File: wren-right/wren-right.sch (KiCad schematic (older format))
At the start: 93 parts, among them J1 TRRS_Jack, SW0 Reset, U1 ProMicro

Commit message: Tracks Finished
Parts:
- MX41: footprint MX_Only:MX-2U -> MX_Only:MX-2U-FLIPPED-ReversedStabilizers
- SW0: footprint random-keyboard-parts:SKQG-1155865 -> Button_Switch_THT:SW_PUSH_6mm
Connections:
- net COL0: now also U1.13 (D10(PB6)); no longer U1.20 (A3(PF4))
- net COL1: now also U1.14 (D16(PB2)); no longer U1.19 (A2(PF5))
- net COL2: now also U1.15 (D14(PB3)); no longer U1.18 (A1(PF6))
- net COL3: now also U1.16 (D15(PB1)); no longer U1.17 (A0(PF7))
- net COL4: now also U1.17 (A0(PF7)); no longer U1.16 (D15(PB1))
- net COL5: now also U1.18 (A1(PF6)); no longer U1.15 (D14(PB3))
- net COL6: now also U1.19 (A2(PF5)); no longer U1.14 (D16(PB2))
- net COL7: now also U1.20 (A3(PF4)); no longer U1.13 (D10(PB6))
- net COL8: now also U1.9 (D6(PD7)); no longer U1.1 (TX(PD3))
- net COL9: now also U1.10 (D7(PE6)); no longer U1.2 (RX(PD2))
- net ROW0: now also U1.1 (TX(PD3)); no longer U1.7 (D4(PD4))
- net ROW1: now also U1.2 (RX(PD2)); no longer U1.8 (D5(PC6))
- net ROW2: now also U1.7 (D4(PD4)); no longer U1.9 (D6(PD7))
- net ROW3: now also U1.8 (D5(PC6)); no longer U1.10 (D7(PE6))
- net ROW4: now also U1.12 (D9(PB5)); no longer U1.11 (D8(PB4))
- no-connect marks 1 -> 2
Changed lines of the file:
@@
 Text GLabel 1950 3150 0    50   BiDi ~ 0
-SCL
-Text GLabel 3950 4250 2    50   BiDi ~ 0
-SDA
-Text GLabel 3950 4350 2    50   BiDi ~ 0
 SCL
 Text GLabel 3250 2950 2    50   Output ~ 0
@@
 	1    0    0    -1
 $EndComp
-$Comp
-L Device:R_Small R2
-U 1 1 6072E460
-P 3500 4450
-F 0 "R2" H 3559 4496 50  0000 L CNN
-F 1 "10kOhms" H 3559 4405 50  0000 L CNN
-F 2 "Resistor_SMD:R_0805_2012Metric" H 3500 4450 50  0001 C CNN
-F 3 "~" H 3500 4450 50  0001 C CNN
-	1    3500 4450
-	1    0    0    -1
-$EndComp
 Wire Wire Line
 	2850 4450 3000 4450
@@
 F 0 "SW0" H 3750 3135 50  0000 C CNN
 F 1 "Reset" H 3750 3044 50  0000 C CNN
-F 2 "random-keyboard-parts:SKQG-1155865" H 3750 3050 50  0001 C CNN
+F 2 "Button_Switch_THT:SW_PUSH_6mm" H 3750 3050 50  0001 C CNN
 F 3 "~" H 3750 3050 50  0001 C CNN
 	1    3750 2850
@@
 F 0 "MX41" H 5133 5773 60  0000 C CNN
 F 1 "MX-NoLED" H 5133 5699 20  0000 C CNN
-F 2 "MX_Only:MX-2U" H 4475 5525 60  0001 C CNN
+F 2 "MX_Only:MX-2U-FLIPPED-ReversedStabilizers" H 4475 5525 60  0001 C CNN
 F 3 "" H 4475 5525 60  0001 C CNN
 	1    5100 5550
@@
 Text GLabel 9750 2350 1    50   Input ~ 0
 COL9
+Text GLabel 3250 3750 2    50   Input ~ 0
+COL0
+Text GLabel 3250 3650 2    50   Input ~ 0
+COL1
+Text GLabel 3250 3550 2    50   Input ~ 0
+COL2
+Text GLabel 3250 3450 2    50   Input ~ 0
+COL3
+Text GLabel 3250 3350 2    50   Input ~ 0
+COL4
+Text GLabel 3250 3250 2    50   Input ~ 0
+COL5
+Text GLabel 3250 3150 2    50   Input ~ 0
+COL6
 Text GLabel 3250 3050 2    50   Input ~ 0
-COL0
-Text GLabel 3250 3150 2    50   Input ~ 0
-COL1
-Text GLabel 3250 3250 2    50   Input ~ 0
-COL2
-Text GLabel 3250 3350 2    50   Input ~ 0
-COL3
-Text GLabel 3250 3450 2    50   Input ~ 0
-COL4
-Text GLabel 3250 3550 2    50   Input ~ 0
-COL5
-Text GLabel 3250 3650 2    50   Input ~ 0
-COL6
-Text GLabel 3250 3750 2    50   Input ~ 0
 COL7
+Text GLabel 1950 3450 0    50   Input ~ 0
+COL8
+Text GLabel 1950 3550 0    50   Input ~ 0
+COL9
 Text GLabel 1950 2650 0    50   Input ~ 0
-COL8
+ROW0
 Text GLabel 1950 2750 0    50   Input ~ 0
-COL9
+ROW1
 Text GLabel 1950 3250 0    50   Input ~ 0
-ROW0
+ROW2
 Text GLabel 1950 3350 0    50   Input ~ 0
-ROW1
-Text GLabel 1950 3450 0    50   Input ~ 0
-ROW2
-Text GLabel 1950 3550 0    50   Input ~ 0
 ROW3
-Text GLabel 1950 3650 0    50   Input ~ 0
+Text GLabel 1950 3750 0    50   Input ~ 0
 ROW4
-NoConn ~ 1950 3750
+NoConn ~ 1950 3650
+NoConn ~ 1850 4650
+$Comp
+L Device:R_Small R2
+U 1 1 6072E460
+P 3500 4450
+F 0 "R2" H 3559 4496 50  0000 L CNN
+F 1 "10kOhms" H 3559 4405 50  0000 L CNN
+F 2 "Resistor_SMD:R_0805_2012Metric" H 3500 4450 50  0001 C CNN
+F 3 "~" H 3500 4450 50  0001 C CNN
+	1    3500 4450
+	1    0    0    -1
+$EndComp
+Text GLabel 3950 4350 2    50   BiDi ~ 0
+SCL
+Text GLabel 3950 4250 2    50   BiDi ~ 0
+SDA
 $EndSCHEMATC

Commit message: Left Side Finished
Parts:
- removed D10, D17, D18, D19, D20, D27, D28, D29, D30, D37, D38, D39, D40, D7, D8, D9: D_Small, Diode_SMD:D_SOD-123, symbol Device:D_Small
- removed MX10, MX17, MX18, MX19, MX20, MX27, MX28, MX29, MX30, MX37, MX38, MX39, MX40, MX7, MX8, MX9: MX-NoLED, MX_Only:MX-1U, symbol MX_Alps_Hybrid:MX-NoLED
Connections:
- net ROW4: no longer U1.12 (D9(PB5))
- net COL6: no longer names the net of U1.19 (A2(PF5))
- net COL7: no longer names the net of U1.20 (A3(PF4))
- net COL8: no longer names the net of U1.9 (D6(PD7))
- net COL9: no longer names the net of U1.10 (D7(PE6))
- no-connect marks 2 -> 6

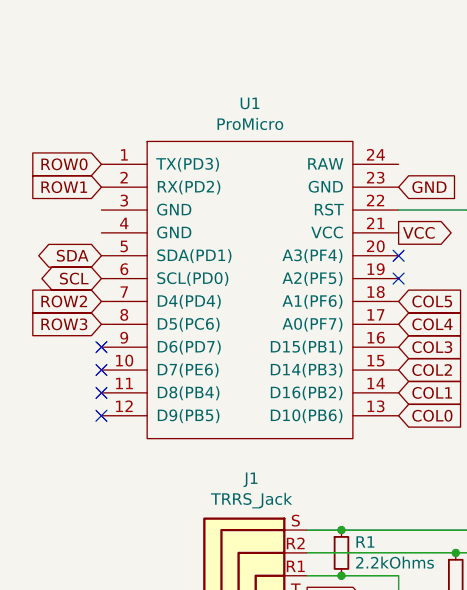
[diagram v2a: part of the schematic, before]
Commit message: Added Mirrored Right PCB
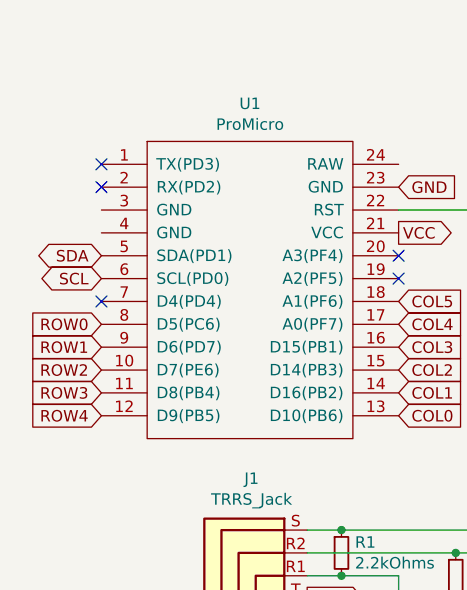
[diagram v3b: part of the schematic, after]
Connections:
- net ROW0: now also U1.8 (D5(PC6)); no longer U1.1 (TX(PD3))
- net ROW1: now also U1.9 (D6(PD7)); no longer U1.2 (RX(PD2))
- net ROW2: now also U1.10 (D7(PE6)); no longer U1.7 (D4(PD4))
- net ROW3: now also U1.11 (D8(PB4)); no longer U1.8 (D5(PC6))
- net ROW4: now also U1.12 (D9(PB5))
- no-connect marks 6 -> 5
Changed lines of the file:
@@
 Text GLabel 3250 3350 2    50   Input ~ 0
 COL4
-Text GLabel 3250 3250 2    50   Input ~ 0
-COL5
-Text GLabel 1950 2650 0    50   Input ~ 0
-ROW0
-Text GLabel 1950 2750 0    50   Input ~ 0
-ROW1
-Text GLabel 1950 3250 0    50   Input ~ 0
+Text GLabel 1950 3550 0    50   Input ~ 0
 ROW2
-Text GLabel 1950 3350 0    50   Input ~ 0
+Text GLabel 1950 3650 0    50   Input ~ 0
 ROW3
-NoConn ~ 1950 3650
+Text GLabel 1950 3750 0    50   Input ~ 0
+ROW4
 $Comp
 L Device:R_Small R2
@@
 Text GLabel 3950 4250 2    50   BiDi ~ 0
 SDA
+Text GLabel 1950 3450 0    50   Input ~ 0
+ROW1
+Text GLabel 1950 3350 0    50   Input ~ 0
+ROW0
+Text GLabel 3250 3250 2    50   Input ~ 0
+COL5
+NoConn ~ 3250 3150
 NoConn ~ 3250 3050
-NoConn ~ 3250 3150
-NoConn ~ 1950 3750
-NoConn ~ 1950 3550
-NoConn ~ 1950 3450
+NoConn ~ 1950 3250
+NoConn ~ 1950 2750
+NoConn ~ 1950 2650
 $EndSCHEMATC

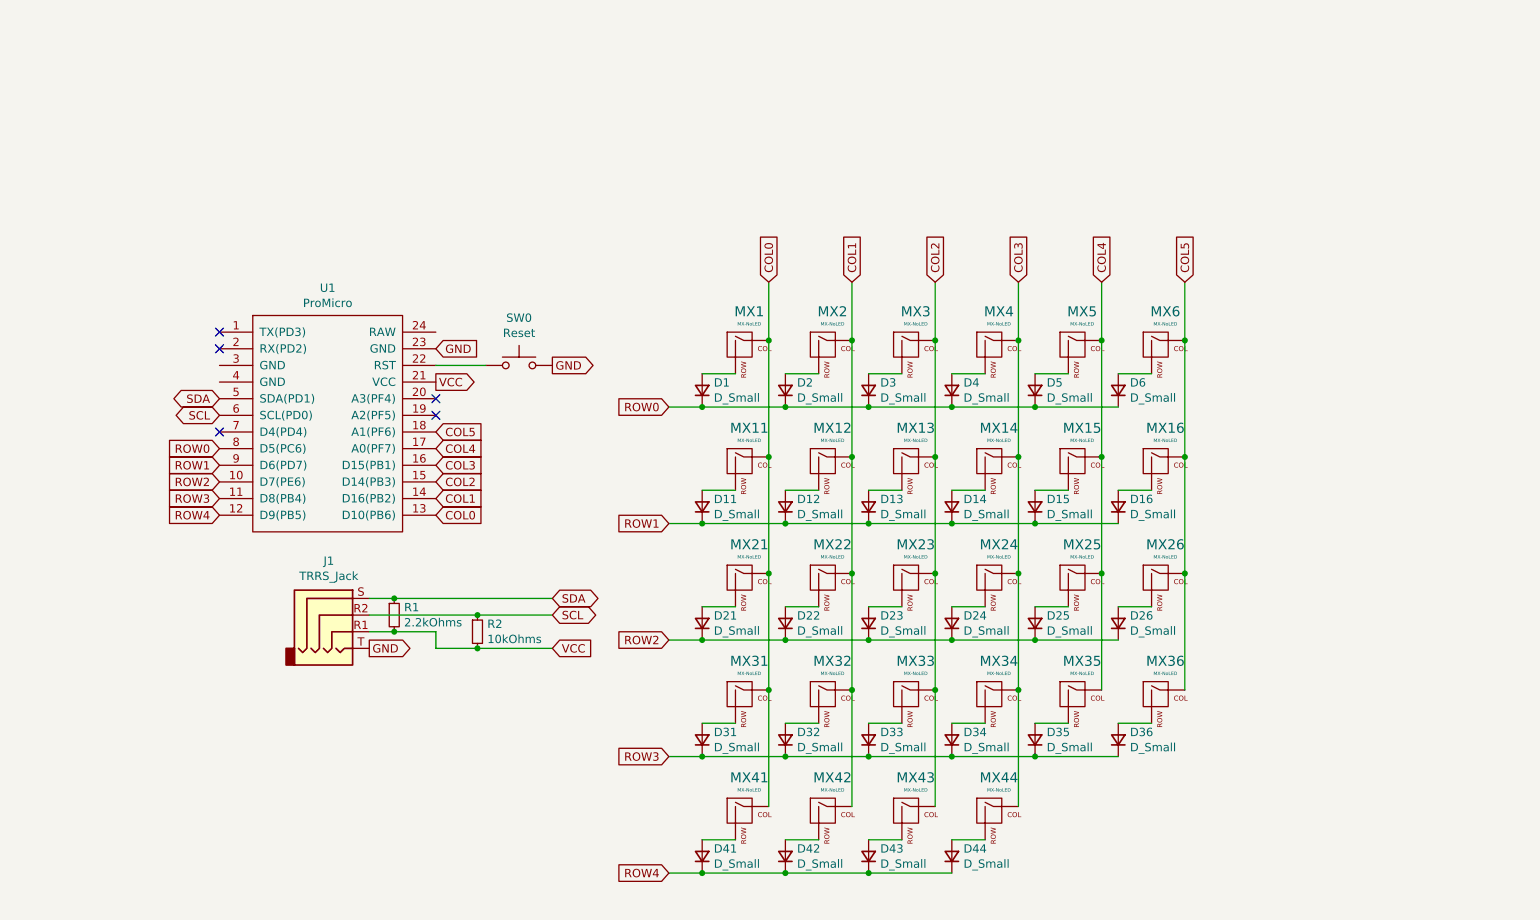
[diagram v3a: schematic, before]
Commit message: Add encoder to right side of schematic
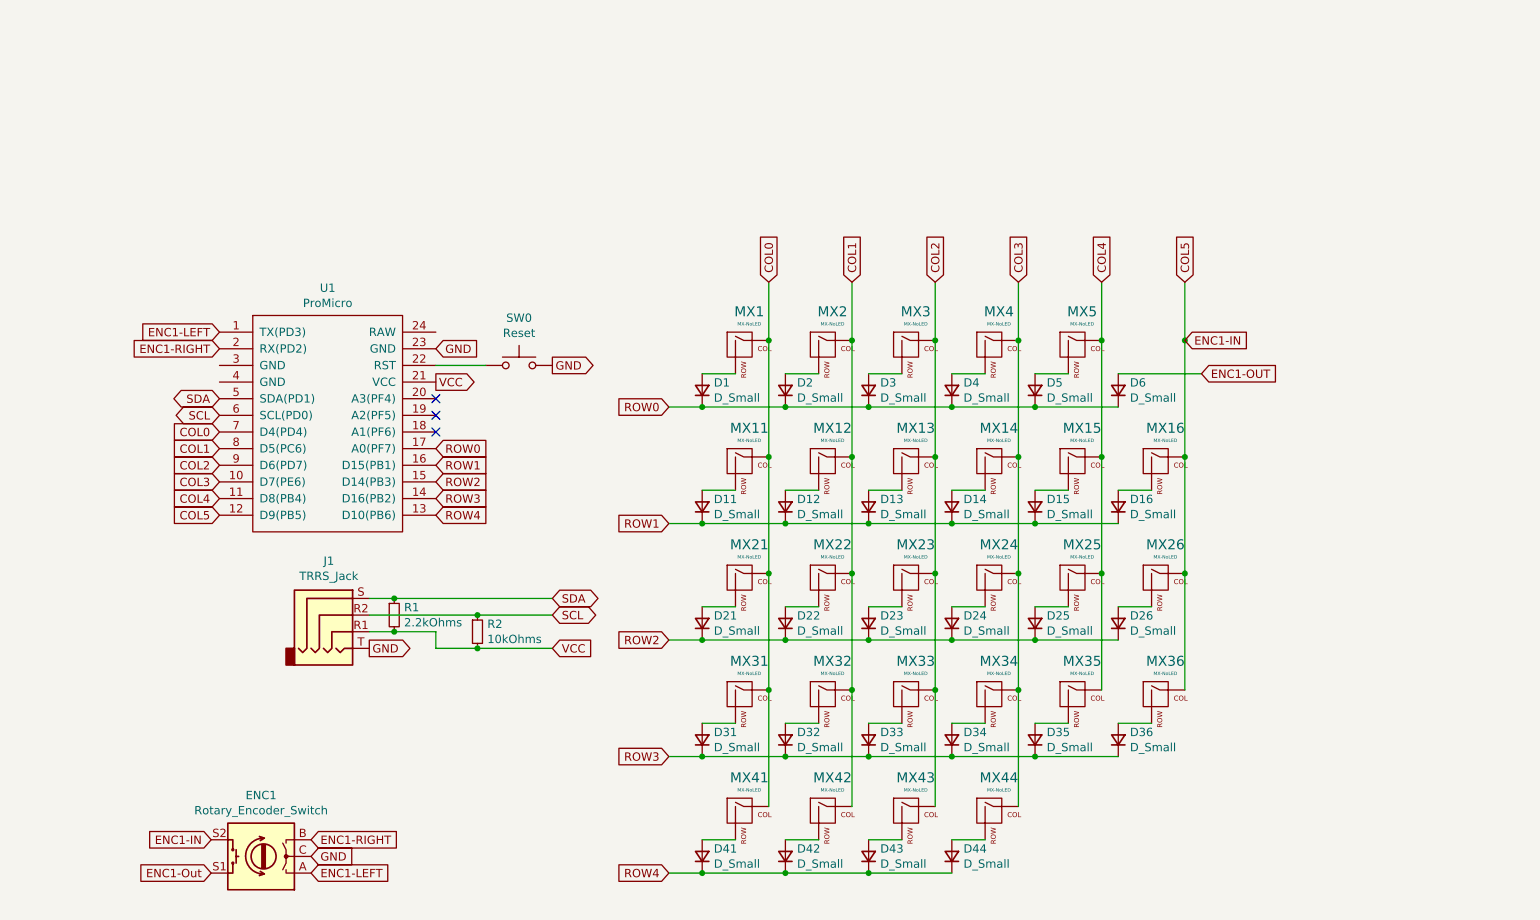
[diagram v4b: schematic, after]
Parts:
- removed MX6: MX-NoLED, MX_Only:MX-1U, symbol MX_Alps_Hybrid:MX-NoLED
- added ENC1: Rotary_Encoder_Switch, symbol Device:Rotary_Encoder_Switch
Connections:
- net COL0: now also U1.7 (D4(PD4)); no longer U1.13 (D10(PB6))
- net COL1: now also U1.8 (D5(PC6)); no longer U1.14 (D16(PB2))
- net COL2: now also U1.9 (D6(PD7)); no longer U1.15 (D14(PB3))
- net COL3: now also U1.10 (D7(PE6)); no longer U1.16 (D15(PB1))
- net COL4: now also U1.11 (D8(PB4)); no longer U1.17 (A0(PF7))
- net COL5: now also U1.12 (D9(PB5)), ENC1.S2; no longer U1.18 (A1(PF6))
- net GND: now also ENC1.C
- net ROW0: now also U1.17 (A0(PF7)); no longer U1.8 (D5(PC6))
- net ROW1: now also U1.16 (D15(PB1)); no longer U1.9 (D6(PD7))
- net ROW2: now also U1.15 (D14(PB3)); no longer U1.10 (D7(PE6))
- net ROW3: now also U1.14 (D16(PB2)); no longer U1.11 (D8(PB4))
- net ROW4: now also U1.13 (D10(PB6)); no longer U1.12 (D9(PB5))
- net ENC1-LEFT: now reaches U1.1 (TX(PD3))
- net ENC1-LEFT: now also ENC1.A
- net ENC1-RIGHT: now reaches U1.2 (RX(PD2))
- net ENC1-RIGHT: now also ENC1.B
- net ENC1-OUT: now reaches D6.2 (A)
- new net ENC1-Out: ENC1.S1
- no-connect marks 5 -> 3
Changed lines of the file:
@@
-	1    0    0    -1
-$EndComp
-$Comp
-L random-keyboard-parts:ProMicro_2 U1
-U 1 1 6071F7CA
-P 2600 3200
-F 0 "U1" H 2600 4015 50  0000 C CNN
-F 1 "ProMicro" H 2600 3924 50  0000 C CNN
-F 2 "footprints:ARDUINO_PRO_MICRO" H 2550 3300 50  0001 C CNN
-F 3 "" H 2550 3300 50  0001 C CNN
-	1    2600 3200
 	1    0    0    -1
 $EndComp
@@
 $EndComp
 $Comp
-L MX_Alps_Hybrid:MX-NoLED MX6
-U 1 1 60752EBC
-P 7600 2750
-F 0 "MX6" H 7633 2973 60  0000 C CNN
-F 1 "MX-NoLED" H 7633 2899 20  0000 C CNN
-F 2 "MX_Only:MX-1U" H 6975 2725 60  0001 C CNN
-F 3 "" H 6975 2725 60  0001 C CNN
-	1    7600 2750
-	1    0    0    -1
-$EndComp
-$Comp
 L MX_Alps_Hybrid:MX-NoLED MX11
 U 1 1 60757491
@@
 	6850 2900 7050 2900
 Wire Wire Line
-	7350 2900 7550 2900
-Wire Wire Line
 	4850 3600 5050 3600
 Wire Wire Line
@@
 Wire Wire Line
 	7250 4100 7250 3400
-Wire Wire Line
-	7750 2350 7750 2700
-Connection ~ 7750 2700
-Wire Wire Line
-	7750 2700 7750 3400
 Connection ~ 7750 3400
 Wire Wire Line
@@
 Text GLabel 7750 2350 1    50   Input ~ 0
 COL5
+Text GLabel 1950 3250 0    50   Input ~ 0
+COL0
+Text GLabel 1950 3350 0    50   Input ~ 0
+COL1
+Text GLabel 1950 3450 0    50   Input ~ 0
+COL2
+Text GLabel 1950 3550 0    50   Input ~ 0
+COL3
+Text GLabel 1950 3650 0    50   Input ~ 0
+COL4
+Text GLabel 3250 3550 2    50   Input ~ 0
+ROW2
+Text GLabel 3250 3650 2    50   Input ~ 0
+ROW3
 Text GLabel 3250 3750 2    50   Input ~ 0
-COL0
-Text GLabel 3250 3650 2    50   Input ~ 0
-COL1
-Text GLabel 3250 3550 2    50   Input ~ 0
-COL2
-Text GLabel 3250 3450 2    50   Input ~ 0
-COL3
-Text GLabel 3250 3350 2    50   Input ~ 0
-COL4
-Text GLabel 1950 3550 0    50   Input ~ 0
-ROW2
-Text GLabel 1950 3650 0    50   Input ~ 0
-ROW3
-Text GLabel 1950 3750 0    50   Input ~ 0
 ROW4
 $Comp
@@
 Text GLabel 3950 4250 2    50   BiDi ~ 0
 SDA
-Text GLabel 1950 3450 0    50   Input ~ 0
+Text GLabel 3250 3450 2    50   Input ~ 0
 ROW1
-Text GLabel 1950 3350 0    50   Input ~ 0
+Text GLabel 3250 3350 2    50   Input ~ 0
 ROW0
-Text GLabel 3250 3250 2    50   Input ~ 0
-COL5
 NoConn ~ 3250 3150
 NoConn ~ 3250 3050
-NoConn ~ 1950 3250
-NoConn ~ 1950 2750
-NoConn ~ 1950 2650
+Text GLabel 1950 3750 0    50   Input ~ 0
+COL5
+$Comp
+L Device:Rotary_Encoder_Switch ENC1
+U 1 1 60751B50
+P 2200 5800
+F 0 "ENC1" H 2200 5433 50  0000 C CNN
+F 1 "Rotary_Encoder_Switch" H 2200 5524 50  0000 C CNN
+F 2 "" H 2050 5960 50  0001 C CNN
+F 3 "~" H 2200 6060 50  0001 C CNN
+	1    2200 5800
+	-1   0    0    1
+$EndComp
+NoConn ~ 3250 3250
+Text GLabel 7750 2700 2    50   Input ~ 0
+ENC1-IN
+Text GLabel 7850 2900 2    50   Input ~ 0
+ENC1-OUT
+Wire Wire Line
+	7350 2900 7850 2900
+Wire Wire Line
+	7750 2350 7750 2700
+Connection ~ 7750 2700
+Wire Wire Line
+	7750 2700 7750 3400
+Text GLabel 1900 5700 0    50   Input ~ 0
+ENC1-IN
+Text GLabel 1900 5900 0    50   Input ~ 0
+ENC1-Out
+Text GLabel 2500 5800 2    50   Input ~ 0
+GND
+Text GLabel 2500 5700 2    50   Input ~ 0
+ENC1-RIGHT
+Text GLabel 2500 5900 2    50   Input ~ 0
+ENC1-LEFT
+$Comp
+L random-keyboard-parts:ProMicro_2 U1
+U 1 1 6071F7CA
+P 2600 3200
+F 0 "U1" H 2600 4015 50  0000 C CNN
+F 1 "ProMicro" H 2600 3924 50  0000 C CNN
+F 2 "footprints:ARDUINO_PRO_MICRO" H 2550 3300 50  0001 C CNN
+F 3 "" H 2550 3300 50  0001 C CNN
+	1    2600 3200
+	1    0    0    -1
+$EndComp
+Text GLabel 1950 2650 0    50   Input ~ 0
+ENC1-LEFT
+Text GLabel 1950 2750 0    50   Input ~ 0
+ENC1-RIGHT
 $EndSCHEMATC

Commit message: Cleaner Track Routing, Remove Encoder
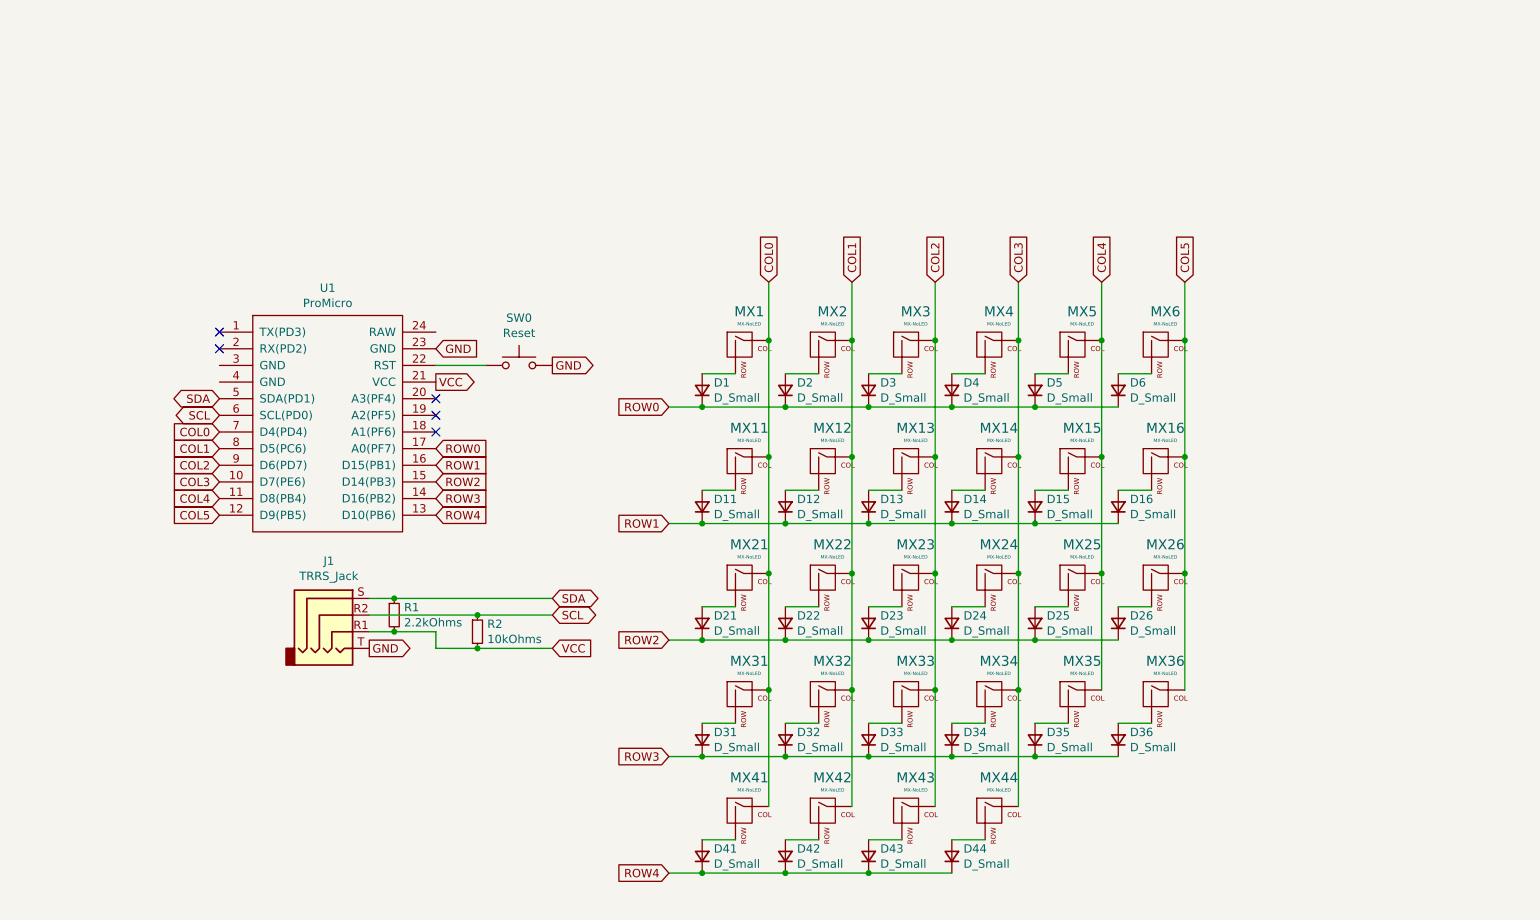
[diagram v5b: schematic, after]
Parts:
- removed ENC1: Rotary_Encoder_Switch, symbol Device:Rotary_Encoder_Switch
- added MX6: MX-NoLED, MX_Only:MX-1U, symbol MX_Alps_Hybrid:MX-NoLED
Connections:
- net COL5: now also MX6.1 (COL)
- net ENC1-LEFT: no longer names the net of U1.1 (TX(PD3))
- net ENC1-OUT: no longer names the net of D6.2 (A)
- net ENC1-OUT: now also MX6.2 (ROW)
- net ENC1-RIGHT: no longer names the net of U1.2 (RX(PD2))
- no-connect marks 3 -> 5
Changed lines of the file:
@@
 Text GLabel 1950 3750 0    50   Input ~ 0
 COL5
-$Comp
-L Device:Rotary_Encoder_Switch ENC1
-U 1 1 60751B50
-P 2200 5800
-F 0 "ENC1" H 2200 5433 50  0000 C CNN
-F 1 "Rotary_Encoder_Switch" H 2200 5524 50  0000 C CNN
-F 2 "" H 2050 5960 50  0001 C CNN
-F 3 "~" H 2200 6060 50  0001 C CNN
-	1    2200 5800
-	-1   0    0    1
-$EndComp
 NoConn ~ 3250 3250
-Text GLabel 7750 2700 2    50   Input ~ 0
-ENC1-IN
-Text GLabel 7850 2900 2    50   Input ~ 0
-ENC1-OUT
-Wire Wire Line
-	7350 2900 7850 2900
-Wire Wire Line
-	7750 2350 7750 2700
-Connection ~ 7750 2700
-Wire Wire Line
-	7750 2700 7750 3400
-Text GLabel 1900 5700 0    50   Input ~ 0
-ENC1-IN
-Text GLabel 1900 5900 0    50   Input ~ 0
-ENC1-Out
-Text GLabel 2500 5800 2    50   Input ~ 0
-GND
-Text GLabel 2500 5700 2    50   Input ~ 0
-ENC1-RIGHT
-Text GLabel 2500 5900 2    50   Input ~ 0
-ENC1-LEFT
 $Comp
 L random-keyboard-parts:ProMicro_2 U1
@@
 	1    0    0    -1
 $EndComp
-Text GLabel 1950 2650 0    50   Input ~ 0
-ENC1-LEFT
-Text GLabel 1950 2750 0    50   Input ~ 0
-ENC1-RIGHT
+Wire Wire Line
+	7750 2350 7750 2700
+$Comp
+L MX_Alps_Hybrid:MX-NoLED MX6
+U 1 1 6073C7A0
+P 7600 2750
+F 0 "MX6" H 7633 2973 60  0000 C CNN
+F 1 "MX-NoLED" H 7633 2899 20  0000 C CNN
+F 2 "MX_Only:MX-1U" H 6975 2725 60  0001 C CNN
+F 3 "" H 6975 2725 60  0001 C CNN
+	1    7600 2750
+	1    0    0    -1
+$EndComp
+Connection ~ 7750 2700
+Wire Wire Line
+	7750 2700 7750 3400
+Wire Wire Line
+	7350 2900 7550 2900
+NoConn ~ 1950 2650
+NoConn ~ 1950 2750
 $EndSCHEMATC
